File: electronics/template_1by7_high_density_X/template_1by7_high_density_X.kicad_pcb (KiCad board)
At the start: 2 copper layers, 19 x 19 mm, 8 parts, among them J1 1, J2 2, J3 3, J4 4, J5 5, J6 6

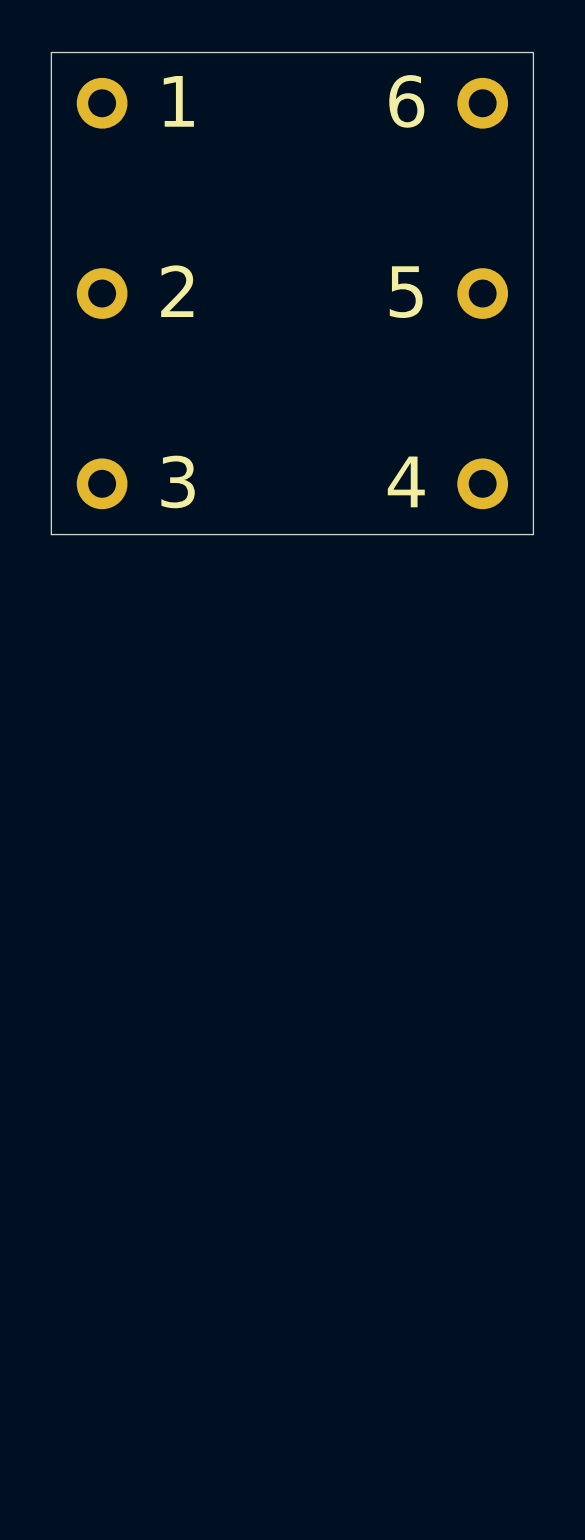
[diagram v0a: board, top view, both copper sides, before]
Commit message: added Kosmos high density X templates and completed high density XN templates
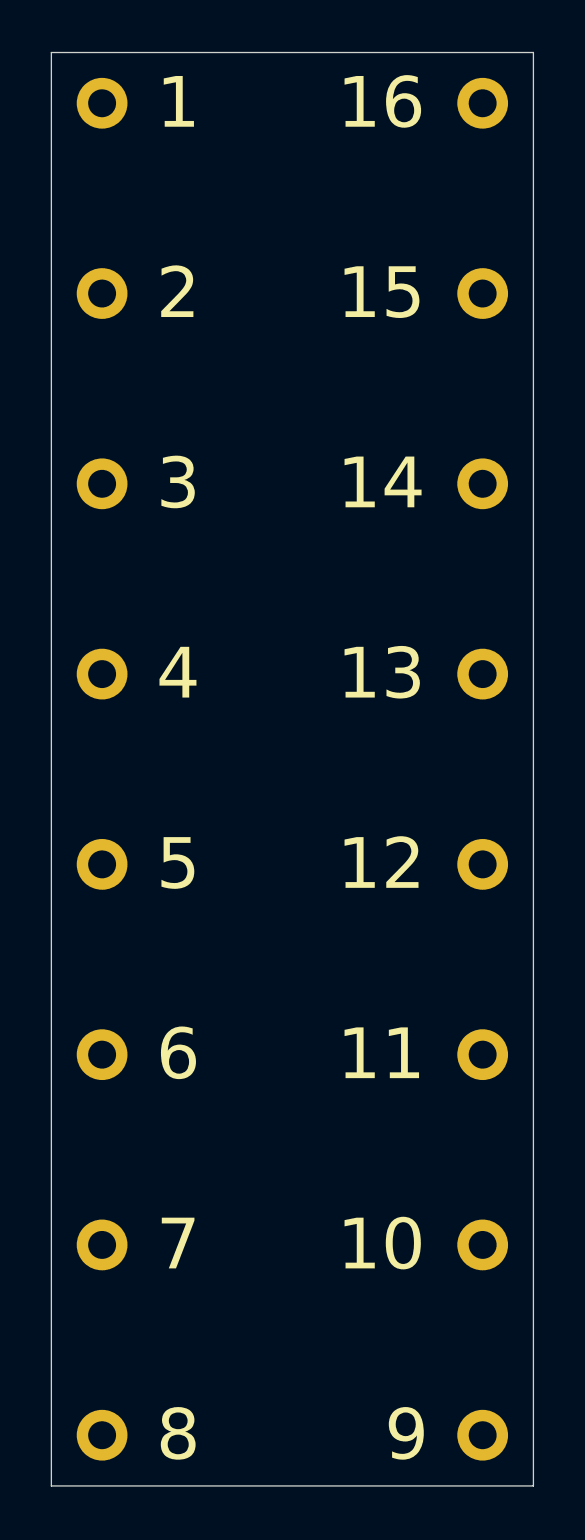
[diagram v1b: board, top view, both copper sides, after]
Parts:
- added J10: 10, mill-max:PC_pin_nail_head_6092, F.Cu at (157.5, 107.5)
- added J11: 11, mill-max:PC_pin_nail_head_6092, F.Cu at (157.5, 100.0)
- added J12: 12, mill-max:PC_pin_nail_head_6092, F.Cu at (157.5, 92.5)
- added J13: 13, mill-max:PC_pin_nail_head_6092, F.Cu at (157.5, 85.0)
- added J14: 14, mill-max:PC_pin_nail_head_6092, F.Cu at (157.5, 77.5)
- added J15: 15, mill-max:PC_pin_nail_head_6092, F.Cu at (157.5, 70.0)
- added J16: 16, mill-max:PC_pin_nail_head_6092, F.Cu at (157.5, 62.5)
- added J7: 7, mill-max:PC_pin_nail_head_6092, F.Cu at (142.5, 107.5)
- added J8: 8, mill-max:PC_pin_nail_head_6092, F.Cu at (142.5, 115.0)
- added J9: 9, mill-max:PC_pin_nail_head_6092, F.Cu at (157.5, 115.0)
- N1: value V20220113 -> V20240506
- moved J6 40.4 mm to (142.5, 100.0), turned to 180 degrees
- moved J5 27.0 mm to (142.5, 92.5), turned to 180 degrees
- moved J4 16.8 mm to (142.5, 85.0), turned to 180 degrees
- moved N1 7.50 mm to (150.9, 80.2)
- moved N2 7.50 mm to (150.0, 76.5)
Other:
- board size 19 x 19 mm -> 19 x 56.5 mm

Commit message: completed high density X templates, updated versionnumbers of high density XN templates
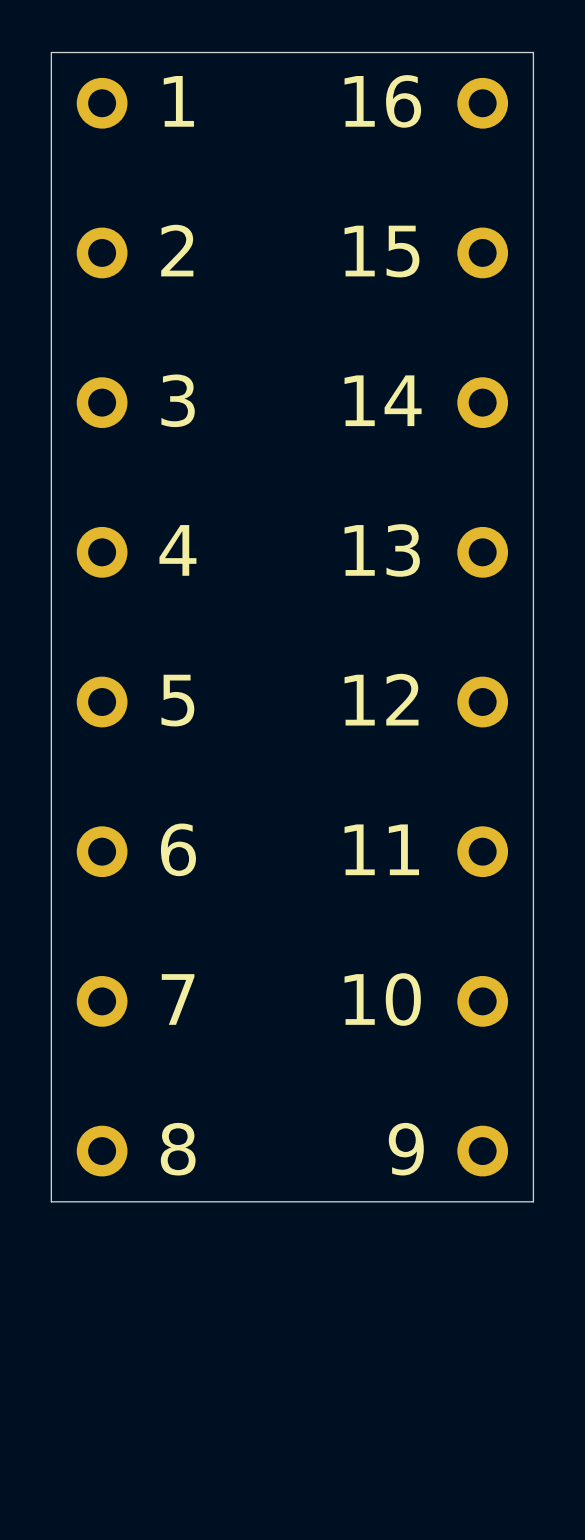
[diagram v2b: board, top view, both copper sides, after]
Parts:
- moved J8 11.2 mm to (142.5, 103.8)
- moved J9 11.2 mm to (157.5, 103.8)
- moved J10 9.60 mm to (157.5, 97.9)
- moved J7 9.60 mm to (142.5, 97.9)
- moved J11 8.00 mm to (157.5, 92.0)
- moved J6 8.00 mm to (142.5, 92.0)
- moved J12 6.40 mm to (157.5, 86.1)
- moved J5 6.40 mm to (142.5, 86.1)
- moved N1 6.10 mm to (150.9, 86.3)
- moved N2 6.10 mm to (150.0, 82.6)
- moved J13 4.80 mm to (157.5, 80.2)
- moved J4 4.80 mm to (142.5, 80.2)
- moved J14 3.20 mm to (157.5, 74.3)
- moved J3 3.20 mm to (142.5, 74.3)
- moved J15 1.60 mm to (157.5, 68.4)
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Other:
- board size 19 x 56.5 mm -> 19 x 45.3 mm
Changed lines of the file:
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@@
   )
   (footprint "mill-max:PC_pin_nail_head_6092" locked (layer "F.Cu")
-    (at 142.5 70)
+    (at 142.5 68.4)
     (property "Sheetfile" "template_1by7.kicad_sch")
     (property "Sheetname" "")
@@
   )
   (footprint "mill-max:PC_pin_nail_head_6092" locked (layer "F.Cu")
-    (at 142.5 77.5)
+    (at 142.5 74.3)
     (property "Sheetfile" "template_1by7.kicad_sch")
     (property "Sheetname" "")
@@
   )
   (footprint "mill-max:PC_pin_nail_head_6092" locked (layer "F.Cu")
-    (at 142.5 92.5 180)
+    (at 142.5 86.1 180)
     (property "Sheetfile" "template_1by7.kicad_sch")
     (property "Sheetname" "")
@@
   )
   (footprint "mill-max:PC_pin_nail_head_6092" locked (layer "F.Cu")
-    (at 142.5 100 180)
+    (at 142.5 92 180)
     (property "Sheetfile" "template_1by7.kicad_sch")
     (property "Sheetname" "")
@@
   )
   (footprint "mill-max:PC_pin_nail_head_6092" locked (layer "F.Cu")
-    (at 142.5 85 180)
+    (at 142.5 80.2 180)
     (property "Sheetfile" "template_1by7.kicad_sch")
     (property "Sheetname" "")
@@
   )
   (footprint "mill-max:PC_pin_nail_head_6092" locked (layer "F.Cu")
-    (at 157.5 100)
+    (at 157.5 92)
     (property "Sheetfile" "template_1by7.kicad_sch")
     (property "Sheetname" "")
@@
   )
   (footprint "mill-max:PC_pin_nail_head_6092" locked (layer "F.Cu")
-    (at 142.5 115)
+    (at 142.5 103.8)
     (property "Sheetfile" "template_1by7.kicad_sch")
     (property "Sheetname" "")
@@
   )
   (footprint "mill-max:PC_pin_nail_head_6092" locked (layer "F.Cu")
-    (at 157.5 77.5)
+    (at 157.5 74.3)
     (property "Sheetfile" "template_1by7.kicad_sch")
     (property "Sheetname" "")
@@
   )
   (footprint "mill-max:PC_pin_nail_head_6092" locked (layer "F.Cu")
-    (at 157.5 107.5)
+    (at 157.5 97.9)
     (property "Sheetfile" "template_1by7.kicad_sch")
     (property "Sheetname" "")
@@
   )
   (footprint "mill-max:PC_pin_nail_head_6092" locked (layer "F.Cu")
-    (at 157.5 85)
+    (at 157.5 80.2)
     (property "Sheetfile" "template_1by7.kicad_sch")
     (property "Sheetname" "")
@@
   )
   (footprint "mill-max:PC_pin_nail_head_6092" locked (layer "F.Cu")
-    (at 142.5 107.5)
+    (at 142.5 97.9)
     (property "Sheetfile" "template_1by7.kicad_sch")
     (property "Sheetname" "")
@@
   )
   (footprint "mill-max:PC_pin_nail_head_6092" locked (layer "F.Cu")
-    (at 157.5 115)
+    (at 157.5 103.8)
     (property "Sheetfile" "template_1by7.kicad_sch")
     (property "Sheetname" "")
@@
   )
   (footprint "mill-max:PC_pin_nail_head_6092" locked (layer "F.Cu")
-    (at 157.5 92.5)
+    (at 157.5 86.1)
     (property "Sheetfile" "template_1by7.kicad_sch")
     (property "Sheetname" "")
@@
   )
   (footprint "mill-max:PC_pin_nail_head_6092" locked (layer "F.Cu")
-    (at 157.5 70)
+    (at 157.5 68.4)
     (property "Sheetfile" "template_1by7.kicad_sch")
     (property "Sheetname" "")
@@
   )
   (footprint "Symbol:OSHW-Symbol_6.7x6mm_SilkScreen" (layer "B.Cu")
-    (at 150 76.5 180)
+    (at 150 82.6 180)
     (descr "Open Source Hardware Symbol")
     (tags "Logo Symbol OSHW")
@@
   )
   (footprint "SquantorLabels:Label_Generic" (layer "B.Cu")
-    (at 150.9 80.2 180)
+    (at 150.9 86.3 180)
     (descr "Label for general purpose use")
     (tags "Label")
@@
       (stroke (width 0.15) (type solid)) (layer "B.SilkS"))
   )
-  (gr_line (start 140.5 117) (end 159.5 117)
+  (gr_line (start 140.5 105.8) (end 159.5 105.8)
     (stroke (width 0.05) (type solid)) (layer "Edge.Cuts"))
-  (gr_line (start 159.5 60.5) (end 159.5 117)
+  (gr_line (start 159.5 60.5) (end 159.5 105.8)
     (stroke (width 0.05) (type solid)) (layer "Edge.Cuts"))
   (gr_line (start 159.5 60.5) (end 140.5 60.5)
     (stroke (width 0.05) (type solid)) (layer "Edge.Cuts"))
-  (gr_line (start 140.5 117) (end 140.5 60.5)
+  (gr_line (start 140.5 105.8) (end 140.5 60.5)
     (stroke (width 0.05) (type solid)) (layer "Edge.Cuts"))
 )
